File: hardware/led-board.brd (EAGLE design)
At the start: 100 x 15.3 mm, 21 parts, among them U1 ATTINY84-20SSU

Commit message: Fully routed and it doesn't fully look like ass!
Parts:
- moved C7 10.1 mm to (95.6, 2.53), turned to 180 degrees
- moved C9 7.37 mm to (45.3, 7.25), flipped to the top, turned to 270 degrees
- moved C6 3.65 mm to (53.2, 11.6), turned to 180 degrees
- moved C1 1.40 mm to (42.9, 7.25)
- moved C8 0.15 mm to (89.4, 2.50), flipped to the top, turned to 0 degrees
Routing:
- net VCC: track 131.1 -> 211.9 mm, vias 3 -> 6
- net N$5: track 0.00 -> 50.7 mm, vias 0 -> 2
- net N$1: track 0.00 -> 4.74 mm, vias 0 -> 1
- net N$7: track 48.3 -> 44.5 mm
- net MOSI: track 80.3 -> 81.4 mm
- net MISO: track 79.9 -> 79.1 mm

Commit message: Finished layout and silkscreen work
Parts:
- added TP_GND: (no value), microbuilder:PAD-1.5X2.0
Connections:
- net GND: now also TP_GND.P$1
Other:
- board text added: "+"
- board text added: "3.3V"
- board text added: "CE"
- board text added: "CSN"
- board text added: "GND"
- board text added: "IRQ"
- board text added: "SCK"
- board text added: "attiny84"
- board text added: "hue chandelier R3 mayhem & chaos 2015"
- board text added: "vcc"
- board text added: "~MISO"
- board text added: "~MOSI"

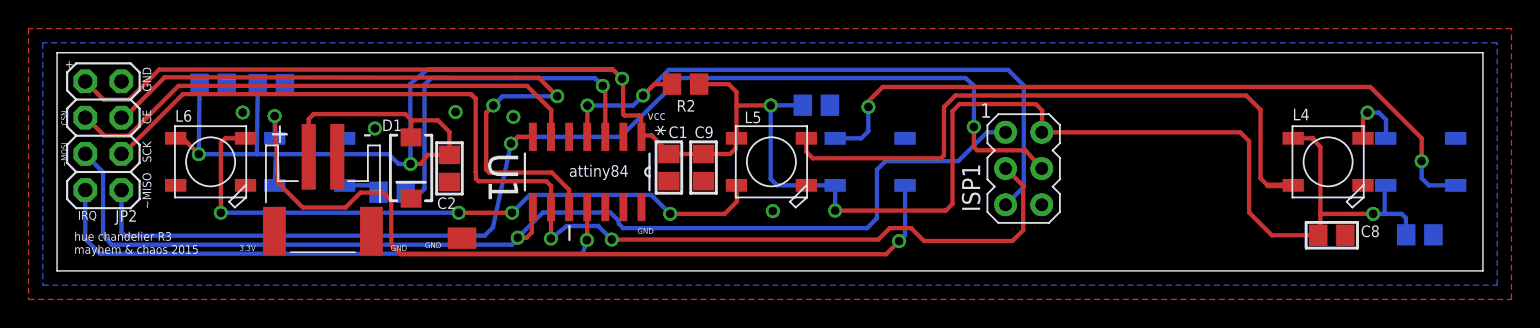
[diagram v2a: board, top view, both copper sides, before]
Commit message: Last version of the arduino code with nurfl stuff. New layout without nurfl.
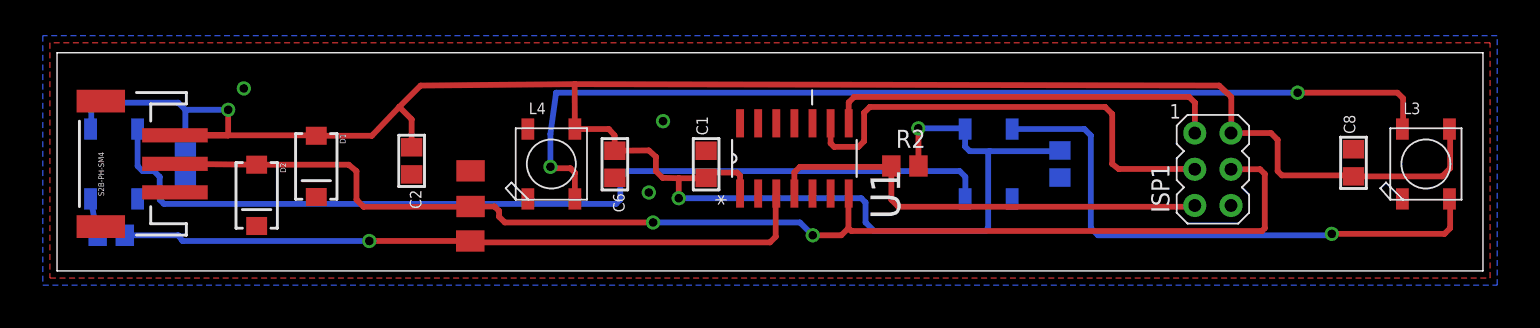
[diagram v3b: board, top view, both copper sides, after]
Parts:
- removed C10, C9: 100nF, microbuilder:0805
- removed JP2: Female socket, adafruit:2X04
- removed L5, L6: WS2812B, adafruit:WS2812B
- added D2: BA340A, SparkFun-DiscreteSemi:SMA-DIODE
- added TP_LED, TP_RX: (no value), microbuilder:PAD-1.5X2.0
- S2B-PH-SM4: value PWR -> 3-PIN SMD; device adafruit:JST-PH-2-SMT-RA -> SparkFun-Connectors:JST-3-SMD
- moved L4 54.5 mm to (34.7, 7.50), turned to 90 degrees
- moved C7 25.7 mm to (70.3, 7.50), turned to 270 degrees
- moved R1 19.9 mm to (3.80, 2.50)
- moved R2 16.4 mm to (59.5, 7.36)
- moved S2B-PH-SM4 15.5 mm to (3.50, 7.50), turned to 90 degrees
- moved C6 14.7 mm to (39.1, 7.48), flipped to the top, turned to 270 degrees
- moved U1 14.6 mm to (51.7, 7.89), turned to 90 degrees
- moved L1 13.7 mm to (4.00, 7.50), turned to 90 degrees
- moved ISP1 13.3 mm to (81.1, 7.13)
- moved L2 8.31 mm to (65.3, 7.50), turned to 90 degrees
- moved C5 8.21 mm to (9.00, 7.50), turned to 270 degrees
- moved D1 6.65 mm to (18.2, 7.33)
- moved C8 5.30 mm to (90.9, 7.58), turned to 90 degrees
- moved TP_GND 4.76 mm to (29.0, 7.02)
- moved C2 2.70 mm to (24.9, 7.72)
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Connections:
- removed net CE: JP2.4, U1.10
- removed net CSN: JP2.3, U1.6
- removed net IRQ: JP2.7, U1.11
- removed net MOSI: ISP1.4, JP2.8, U1.7
- removed net N$3: L5.2-DOUT, L6.4-DIN
- removed net N$7: L4.2-DOUT, L5.4-DIN
- new net DI: D2.A, ISP1.4, S2B-PH-SM4.2, TP_RX.P$1, U1.7
- net GND: now also D2.C, S2B-PH-SM4.1; no longer C10.2, C9.2, JP2.2, L5.3-GND, L6.3-GND, S2B-PH-SM4.2
- net LED: now also TP_LED.P$1
- net MISO: no longer JP2.5
- net SCK: no longer JP2.6
- net VCC: now also S2B-PH-SM4.3; no longer C10.1, C9.1, JP2.1, L5.1-VDD, L6.1-VDD, S2B-PH-SM4.1
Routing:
- net DI: track 0.00 -> 89.0 mm, vias 0 -> 2
- net MOSI: track 81.4 -> 0.00 mm, vias 2 -> 0
- net N$1: track 4.74 -> 70.8 mm, vias 1 -> 2
- net MISO: track 79.1 -> 28.2 mm, vias 1 -> 0
- net CE: track 49.3 -> 0.00 mm, vias 2 -> 0
- net SCK: track 81.6 -> 33.2 mm, vias 2 -> 0
- net N$3: track 45.6 -> 0.00 mm, vias 4 -> 0
- net N$7: track 44.5 -> 0.00 mm
- net IRQ: track 42.1 -> 0.00 mm, vias 1 -> 0
- net CSN: track 37.2 -> 0.00 mm
- net VCC: track 211.9 -> 185.6 mm, vias 6 -> 3
- net LED: track 25.3 -> 49.1 mm
- net RESET: track 45.6 -> 32.4 mm, vias 2 -> 0
- net N$5: track 50.7 -> 39.9 mm, vias 2 -> 1
- net N$2: track 59.0 -> 66.2 mm, vias 2 -> 0
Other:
- board text removed: "+"
- board text removed: "3.3V"
- board text removed: "CE"
- board text removed: "CSN"
- board text removed: "GND"
- board text removed: "IRQ"
- board text removed: "SCK"
- board text removed: "attiny84"
- board text removed: "hue chandelier R3 mayhem & chaos 2015"
- board text removed: "vcc"
- board text removed: "~MISO"
- board text removed: "~MOSI"

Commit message: Basic working node code, updated schematic and layout
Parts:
- added C3: 100nF, microbuilder:0805
- U1: value ATTINY84-20SSU -> ATMEGA168PA-AU; device Atmel_By_element14_Batch_1-00:SOIC127P600X175-14N -> Atmel_By_element14_Batch_1-00:QFP80P900X900X120-32N
- moved R2 16.5 mm to (43.0, 8.01), turned to 180 degrees
- moved C1 3.64 mm to (44.5, 11.0), turned to 180 degrees
- moved U1 0.50 mm to (51.7, 7.39)
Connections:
- removed net DI: D2.A, ISP1.4, S2B-PH-SM4.2, TP_RX.P$1, U1.7
- new net MOSI: ISP1.4, U1.15
- new net RX: D2.A, S2B-PH-SM4.2, TP_RX.P$1, U1.30
- net GND: now also C3.2, U1.21, U1.3, U1.5; no longer U1.14
- net LED: now also U1.32; no longer U1.3
- net MISO: now also U1.16; no longer U1.8
- net RESET: now also C3.1, U1.29; no longer U1.4
- net SCK: now also U1.17; no longer U1.9
- net VCC: now also U1.18, U1.4, U1.6; no longer U1.1
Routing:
- net DI: track 89.0 -> 0.00 mm, vias 2 -> 0
- net RX: track 0.00 -> 45.0 mm
- net MOSI: track 0.00 -> 42.2 mm
- net RESET: track 32.4 -> 40.8 mm, vias 0 -> 2
- net VCC: track 185.6 -> 179.8 mm, vias 3 -> 1
- net MISO: track 28.2 -> 24.0 mm
- net LED: track 49.1 -> 45.4 mm
- net SCK: track 33.2 -> 31.4 mm

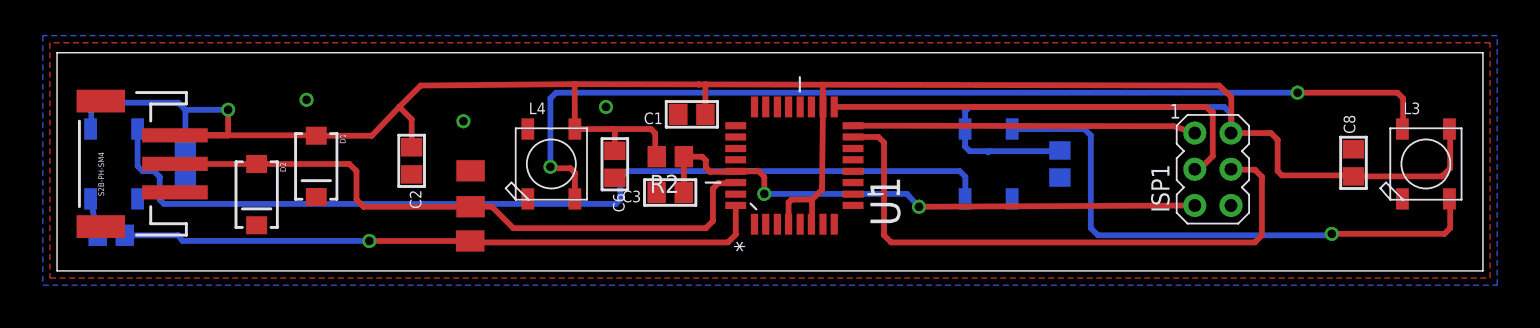
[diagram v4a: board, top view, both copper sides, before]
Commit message: Fixed the orientation of the shottky diodes, improved the layout a bit
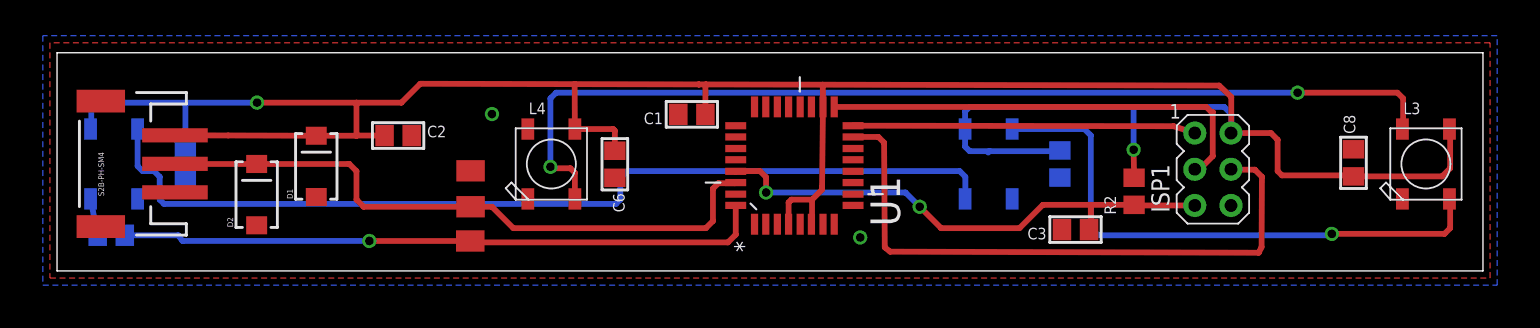
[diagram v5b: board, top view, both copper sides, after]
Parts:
- moved R2 32.6 mm to (75.5, 5.58), turned to 90 degrees
- moved C3 28.5 mm to (71.4, 2.90)
- moved C2 2.01 mm to (23.9, 9.49), turned to 0 degrees
- turned D1 to 90 degrees
- turned D2 to 90 degrees
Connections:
- net GND: now also D1.A, D2.A; no longer D1.C, D2.C
- net RX: now also D2.C; no longer D2.A
- net VCC: now also D1.C; no longer D1.A
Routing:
- net VCC: track 179.8 -> 184.0 mm, vias 1 -> 2
- net RESET: track 40.8 -> 37.1 mm
- net MOSI: track 42.2 -> 43.8 mm

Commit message: Finished layot and silkscreening. Hopefully ready to go!
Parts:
- added TP_RX1: (no value), microbuilder:PAD-1.5X2.0
- moved C7 10.8 mm to (59.8, 10.0), turned to 0 degrees
- moved C5 2.50 mm to (11.0, 9.00)
- moved C8 1.00 mm to (90.9, 8.58)
- renumbered ISP1 to ISP
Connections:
- net VCC: now also TP_RX1.P$1
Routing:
- net VCC: track 184.0 -> 179.4 mm
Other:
- board text added: "5V"
- board text added: "GND"
- board text added: "LED"
- board text added: "LED chandelier, Nowhere 2015 Designed by Mayhem & Chaos"
- board text added: "PWR"
- board text added: "RX"
- board text added: "VCC"
- board text added: "r4"

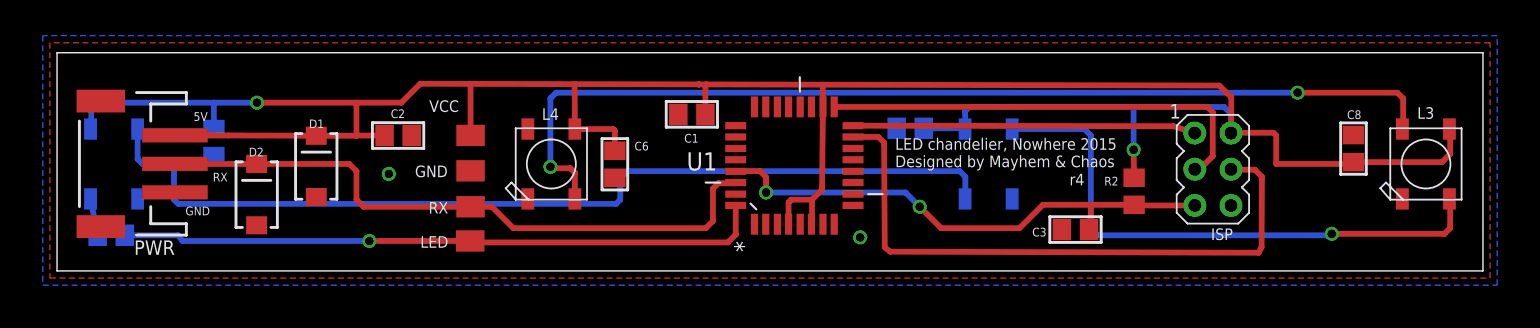
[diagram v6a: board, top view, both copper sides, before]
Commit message: Updated based on Bernard's feedback: Moved parts from the back to the front and moved one via out from under the mcu. Also ensured that no parts are close to the edges.
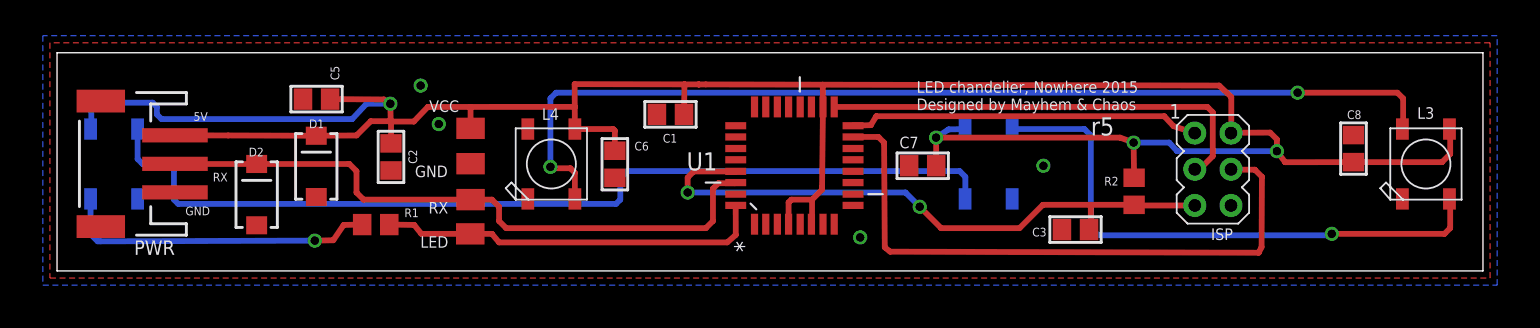
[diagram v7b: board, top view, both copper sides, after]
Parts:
- moved R1 18.6 mm to (22.4, 3.25), flipped to the top, turned to 180 degrees
- moved C5 7.82 mm to (18.2, 12.1), flipped to the top, turned to 180 degrees
- moved C7 2.77 mm to (60.7, 7.38), flipped to the top, turned to 180 degrees
- moved C2 1.58 mm to (23.4, 8.00), turned to 270 degrees
- moved C1 1.50 mm to (43.0, 11.0)
- moved TP_GND 0.50 mm to (29.0, 7.52)
- moved TP_LED 0.50 mm to (29.0, 2.60)
- moved TP_RX 0.50 mm to (29.0, 5.00)
- moved TP_RX1 0.50 mm to (29.0, 10.0)
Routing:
- net N$8: track 2.60 -> 22.3 mm, vias 0 -> 1
- net LED: track 45.4 -> 27.1 mm, vias 1 -> 0
- net RESET: track 37.1 -> 43.8 mm
- net VCC: track 179.4 -> 183.1 mm, vias 2 -> 4
- net MISO: track 24.0 -> 24.7 mm
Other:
- board text added: "r5"
- board text removed: "r4"

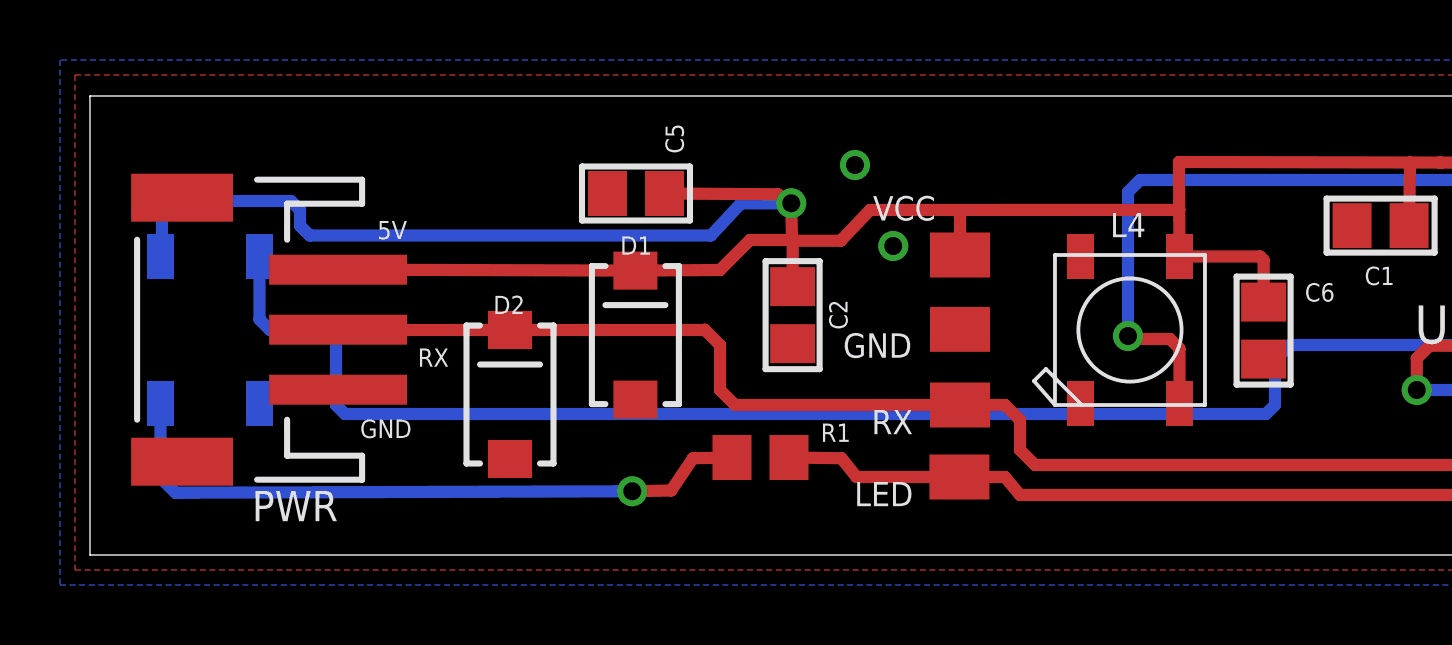
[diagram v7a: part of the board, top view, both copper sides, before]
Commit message: Added mounting holes. Might be done now!
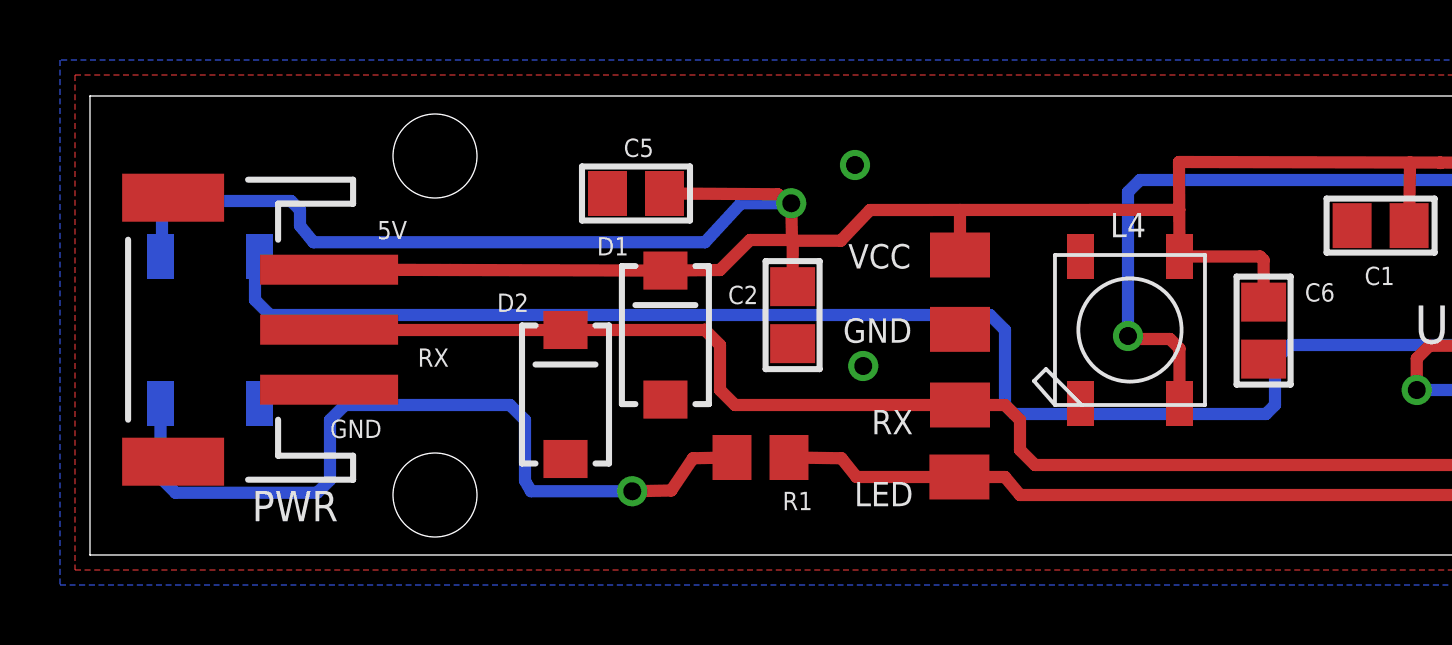
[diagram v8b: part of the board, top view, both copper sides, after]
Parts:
- moved D2 1.85 mm to (15.8, 5.35)
- moved D1 1.00 mm to (19.2, 7.33)
- moved S2B-PH-SM4 0.30 mm to (3.20, 7.50)
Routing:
- net N$8: track 22.3 -> 27.1 mm
- net VCC: track 183.1 -> 183.6 mm
